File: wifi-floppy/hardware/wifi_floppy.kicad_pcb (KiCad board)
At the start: 2 copper layers, 96 x 62 mm, 13 parts, among them J1 FLOPPY34, J2 PWR-BERG, Q1 BSS138, Q2 BSS138, Q3 BSS138, Q4 BSS138, Q5 BSS138, Q6 BSS138, U1 Pico2W/PicoPlus2W, U2 74LVC541A

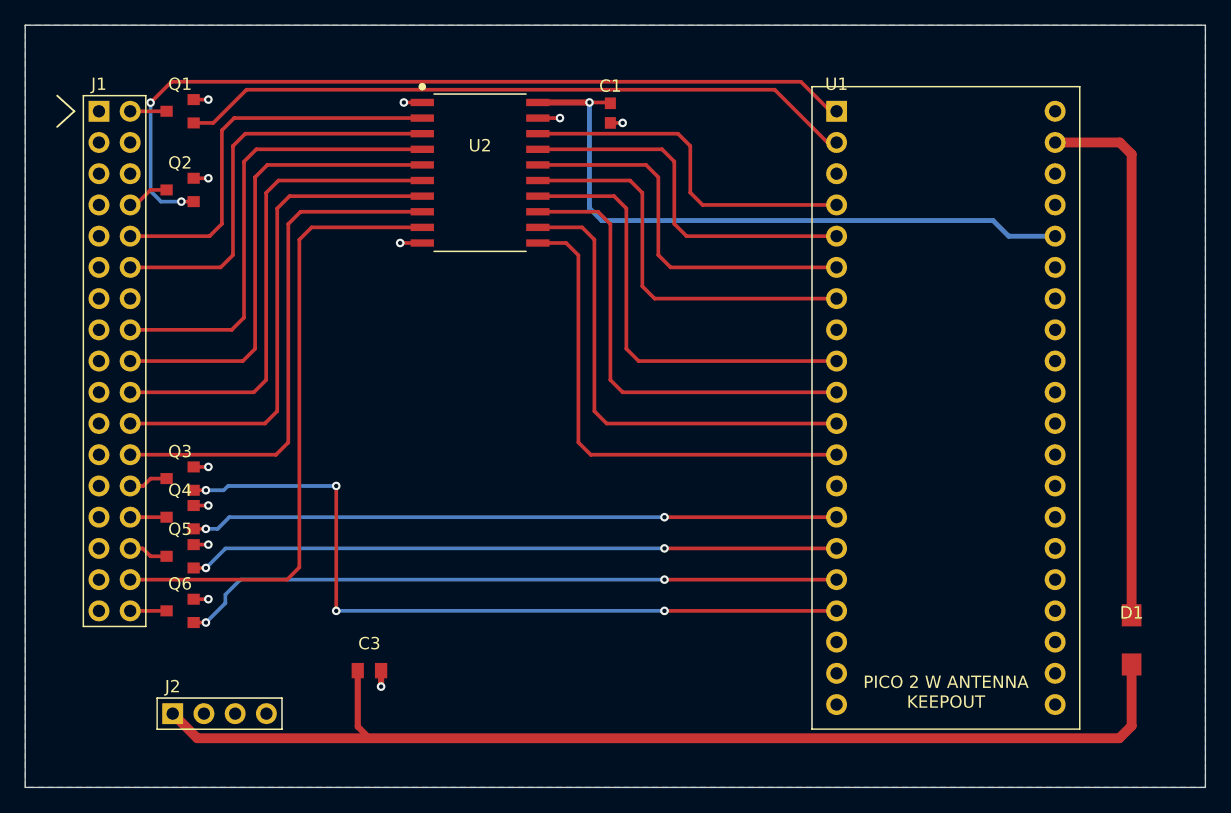
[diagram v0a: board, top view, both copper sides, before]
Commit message: Make rev B: keepout at the antenna end, and a silkscreen that prints
Three fab-output faults, none of which any check was looking at. Rev A came
back mirrored, rev A2 came back with the ground pour under the RM2 antenna,
and both batches came back with a completely blank top side.

Antenna keepout. export_gerbers.py flipped Y for pads, traces, silk, outline
and drill but not for the keepout zone polygon, so the void landed over U1
pins 1/2/39/40 instead of 19-22. The fix arrived on a working copy of the
hardware scripts that predated 0e7f684 - hardcoded /home/claude paths back,
verify_board.py down to 2 of its 7 reference footprints, and the "N footprints
were NOT checked" counter gone. Re-applied onto the committed versions instead,
so none of that is lost.

Silkscreen. Two independent causes. Every silk feature was 0.12 mm (or 0.15,
which is still short of JLCPCB's 6 mil = 0.1524 mm), so the fab stripped the
layer; and export_gerbers.py read only fp_line, so all 13 reference
designators, the keepout label and U2's pin-1 dot never reached the .GTO at
all. Silk is now 0.2 mm and text 1.0-1.5 mm, and stroke_font.py - a
single-stroke vector font - gives the exporter text at last. Designator
placement moved to suit: the FET column is on a 3.14 mm pitch, so a label above
Q4 or Q5 lands on the pads of the FET above it, and all six go east instead.

The board is marked. Rev A and rev A2 carry no revision and no designators, so
the only way to tell a scrap board from a good one was to squint at which end
the pour void sits. It now says WIFI FLOPPY REV B on the silkscreen.

Checks, all reading the emitted Gerbers rather than re-deriving from the
exporter - re-deriving is how the keepout audit agreed with the exporter's own
mistake:
  - the keepout void is at the antenna end and not the other one
  - no silk feature is below the fab's minimum width, and the layer is not
    empty
  - export_gerbers.py reports any legend stroke within 0.15 mm of a pad
  - stroke_font.unsuppor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
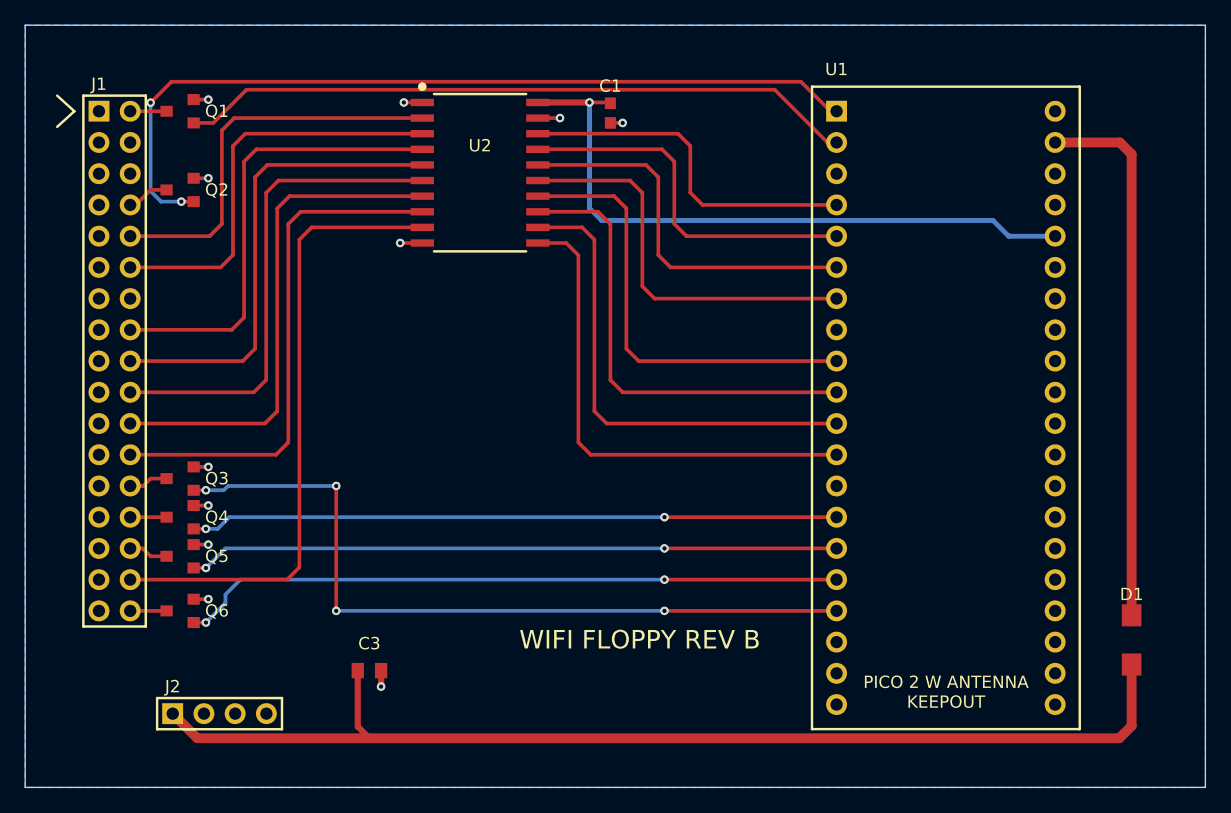
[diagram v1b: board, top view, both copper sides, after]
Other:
- board text added: "WIFI FLOPPY REV B"
